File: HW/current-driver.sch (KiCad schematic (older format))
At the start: 20 parts, among them P1 IN+, P2 IN-, P3 LED, P4 SW_IN, P5 SENSE, P6 OUT+, P7 OUT-, Q1 IRFZ44VBF, U1 INA168

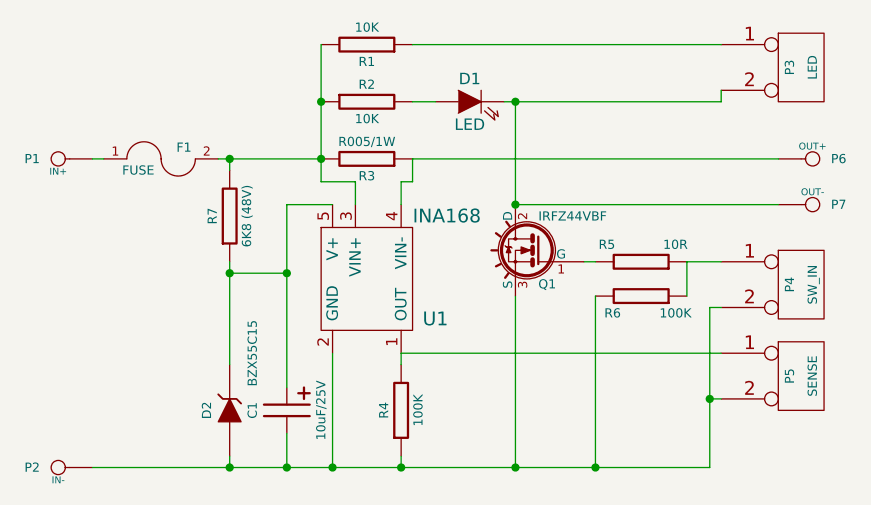
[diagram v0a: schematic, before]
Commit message: MOSTFET changed to a logic drive one
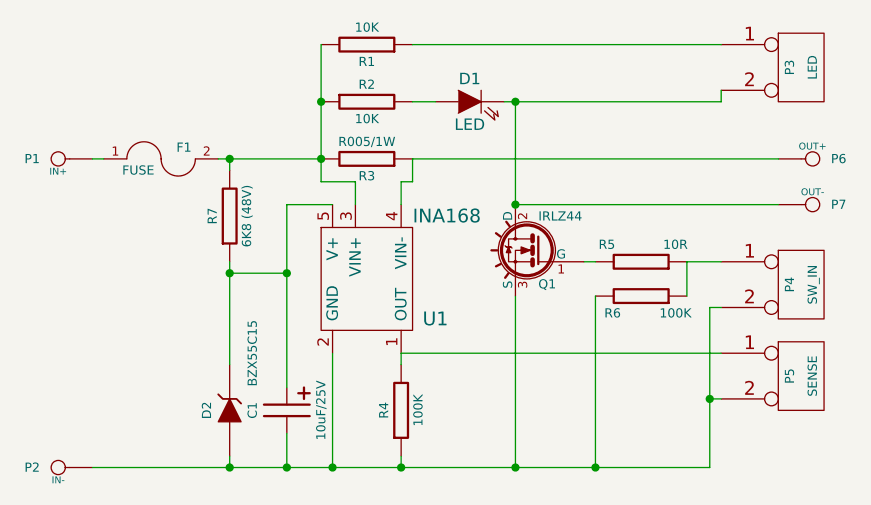
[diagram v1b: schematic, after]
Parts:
- Q1: value IRFZ44VBF -> IRLZ44
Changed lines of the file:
@@
 Sheet 1 1
 Title ""
-Date "30 jul 2014"
+Date "6 aug 2014"
 Rev ""
 Comp ""
@@
 P 4700 2550
 F 0 "Q1" H 4700 2402 40  0000 R CNN
-F 1 "IRFZ44VBF" H 4700 2699 40  0000 R CNN
+F 1 "IRLZ44" H 4700 2699 40  0000 R CNN
 F 2 "TO220" H 4521 2651 29  0001 C CNN
 F 3 "~" H 4700 2550 60  0000 C CNN
